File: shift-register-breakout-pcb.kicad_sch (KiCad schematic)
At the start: 19 parts, among them J1 Conn_01x07_Socket, J2 Conn_01x08_Socket, J3 Conn_01x08_Socket, J4 Conn_01x08_Socket, J5 Conn_01x08_Socket

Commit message: adding text, fixing some errors.
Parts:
- added LOGO1, LOGO4: **REF, ct-kicad:awesome-logo, symbol ct-kicad:awesome-logo
- added LOGO2, LOGO3: **REF, ct-kicad:qmk-lite, symbol ct-kicad:qmk-lite-logo
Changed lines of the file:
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@@
+    )
+  )
+  (symbol (lib_id "ct-kicad:qmk-lite-logo") (at 55.88 26.67 0) (unit 1)
+    (in_bom no) (on_board yes) (dnp no) (fields_autoplaced)
+    (property "Reference" "LOGO2" (at 58.42 25.4 0)
+      (effects (font (size 1.27 1.27)) (justify left))
+    )
+    (property "Value" "**REF" (at 58.42 27.94 0)
+      (effects (font (size 1.27 1.27)) (justify left))
+    )
+    (property "Footprint" "ct-kicad:qmk-lite" (at 55.88 26.67 0)
+      (effects (font (size 1.27 1.27)) hide)
+    )
+    (property "Datasheet" "" (at 55.88 26.67 0)
+      (effects (font (size 1.27 1.27)) hide)
+    )
+    (instances
+      (project "shift-register-breakout-pcb"
+        (path "/3deab8a1-c8b9-4932-a4cb-ae1a41e6ee5f"
+          (reference "LOGO2") (unit 1)
+        )
+      )
     )
   )
@@
     )
   )
+  (symbol (lib_id "ct-kicad:awesome-logo") (at 67.31 20.32 0) (unit 1)
+    (in_bom no) (on_board yes) (dnp no) (fields_autoplaced)
+    (property "Reference" "LOGO4" (at 69.85 19.05 0)
+      (effects (font (size 1.27 1.27)) (justify left))
+    )
+    (property "Value" "**REF" (at 69.85 21.59 0)
+      (effects (font (size 1.27 1.27)) (justify left))
+    )
+    (property "Footprint" "ct-kicad:awesome-logo" (at 67.31 20.32 0)
+      (effects (font (size 1.27 1.27)) hide)
+    )
+    (property "Datasheet" "" (at 67.31 20.32 0)
+      (effects (font (size 1.27 1.27)) hide)
+    )
+    (instances
+      (project "shift-register-breakout-pcb"
+        (path "/3deab8a1-c8b9-4932-a4cb-ae1a41e6ee5f"
+          (reference "LOGO4") (unit 1)
+        )
+      )
+    )
+  )
   (symbol (lib_id "power:GND") (at 127 102.87 180) (unit 1)
     (in_bom yes) (on_board yes) (dnp no) (fields_autoplaced)
@@
     )
   )
+  (symbol (lib_id "ct-kicad:awesome-logo") (at 55.88 20.32 0) (unit 1)
+    (in_bom no) (on_board yes) (dnp no) (fields_autoplaced)
+    (property "Reference" "LOGO1" (at 58.42 19.05 0)
+      (effects (font (size 1.27 1.27)) (justify left))
+    )
+    (property "Value" "**REF" (at 58.42 21.59 0)
+      (effects (font (size 1.27 1.27)) (justify left))
+    )
+    (property "Footprint" "ct-kicad:awesome-logo" (at 55.88 20.32 0)
+      (effects (font (size 1.27 1.27)) hide)
+    )
+    (property "Datasheet" "" (at 55.88 20.32 0)
+      (effects (font (size 1.27 1.27)) hide)
+    )
+    (instances
+      (project "shift-register-breakout-pcb"
+        (path "/3deab8a1-c8b9-4932-a4cb-ae1a41e6ee5f"
+          (reference "LOGO1") (unit 1)
+        )
+      )
+    )
+  )
   (symbol (lib_id "Mechanical:MountingHole") (at 22.86 20.32 0) (unit 1)
     (in_bom yes) (on_board yes) (dnp no) (fields_autoplaced)
@@
         )
       )
+    )
+  )
+  (symbol (lib_id "ct-kicad:qmk-lite-logo") (at 67.31 26.67 0) (unit 1)
+    (in_bom no) (on_board yes) (dnp no) (fields_autoplaced)
+    (property "Reference" "LOGO3" (at 69.85 25.4 0)
+      (effects (font (size 1.27 1.27)) (justify left))
+    )
+    (property "Value" "**REF" (at 69.85 27.94 0)
+      (effects (font (size 1.27 1.27)) (justify left))
+    )
+    (property "Footprint" "ct-kicad:qmk-lite" (at 67.31 26.67 0)
+      (effects (font (size 1.27 1.27)) hide)
+    )
+    (property "Datasheet" "" (at 67.31 26.67 0)
+      (effects (font (size 1.27 1.27)) hide)
+    )
+    (instances
+      (project "shift-register-breakout-pcb"
+        (path "/3deab8a1-c8b9-4932-a4cb-ae1a41e6ee5f"
+          (reference "LOGO3") (unit 1)
+        )
+      )

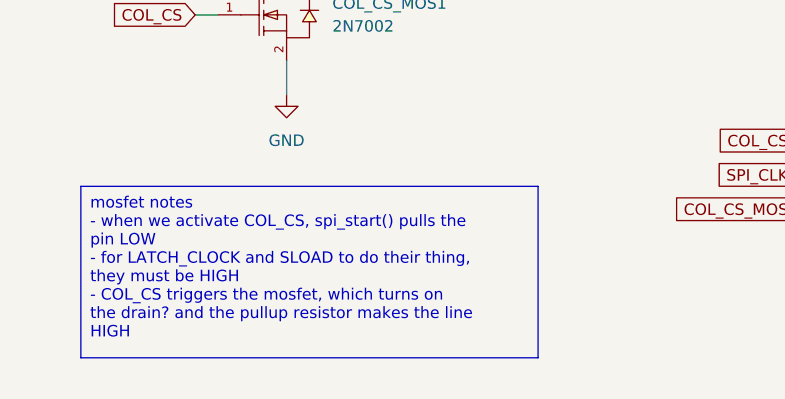
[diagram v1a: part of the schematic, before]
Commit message: fixing mosfet notes in schematic as per burkfers, final pcb notation added
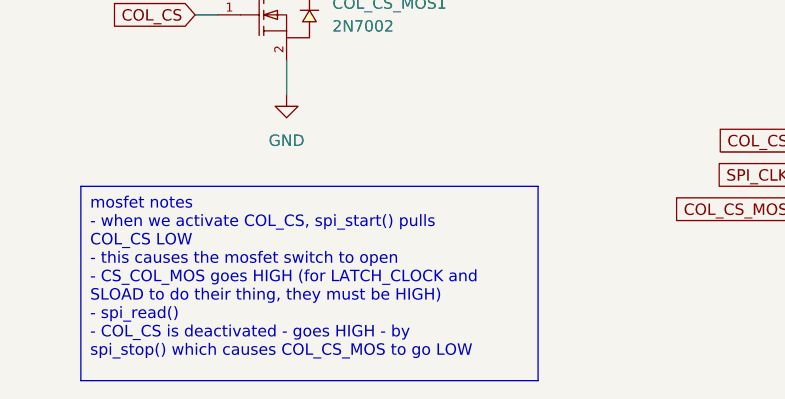
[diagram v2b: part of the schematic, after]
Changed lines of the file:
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@@
     (stroke (width 0) (type default))
   )
-  (text_box "mosfet notes\n- when we activate COL_CS, spi_start() pulls the pin LOW\n- for LATCH_CLOCK and SLOAD to do their thing, they must be HIGH\n- COL_CS triggers the mosfet, which turns on the drain? and the pullup resistor makes the line HIGH"
-    (at 27.94 144.78 0) (size 50.8 19.05)
+  (text_box "mosfet notes\n- when we activate COL_CS, spi_start() pulls COL_CS LOW\n- this causes the mosfet switch to open\n- CS_COL_MOS goes HIGH (for LATCH_CLOCK and SLOAD to do their thing, they must be HIGH)\n- spi_read()\n- COL_CS is deactivated - goes HIGH - by spi_stop() which causes COL_CS_MOS to go LOW"
+    (at 27.94 144.78 0) (size 50.8 21.59)
     (stroke (width 0) (type default))
     (fill (type none))

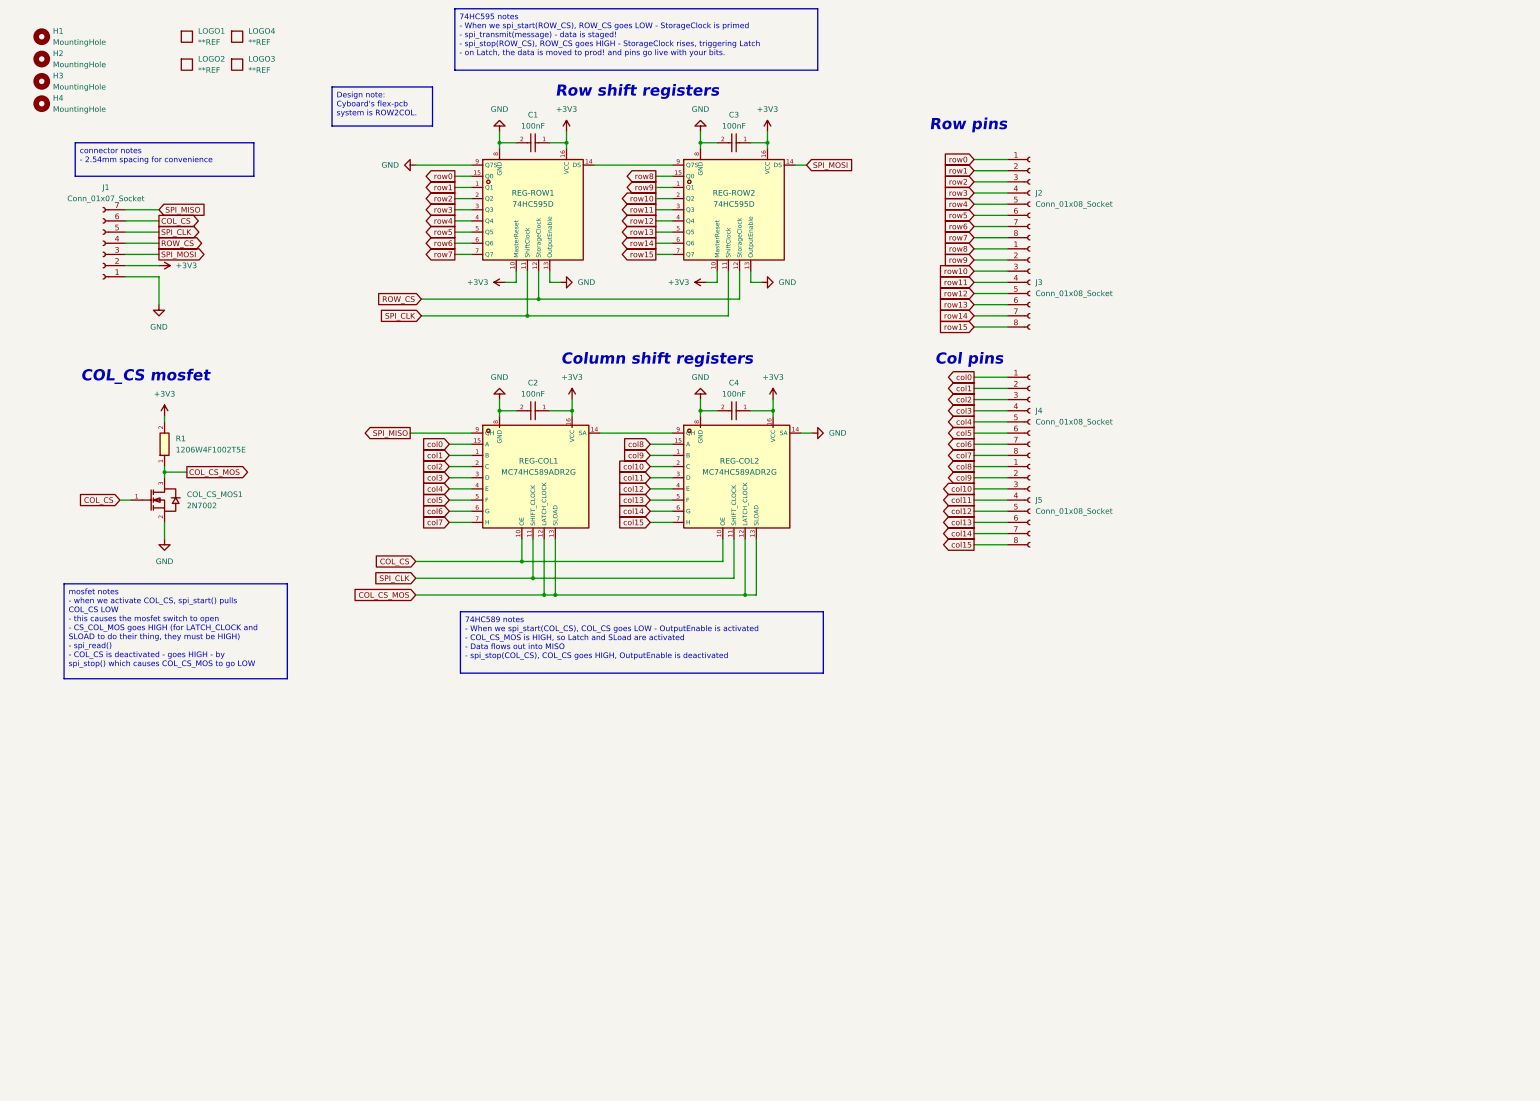
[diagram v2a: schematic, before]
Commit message: adding latch circuit and resistor arrays
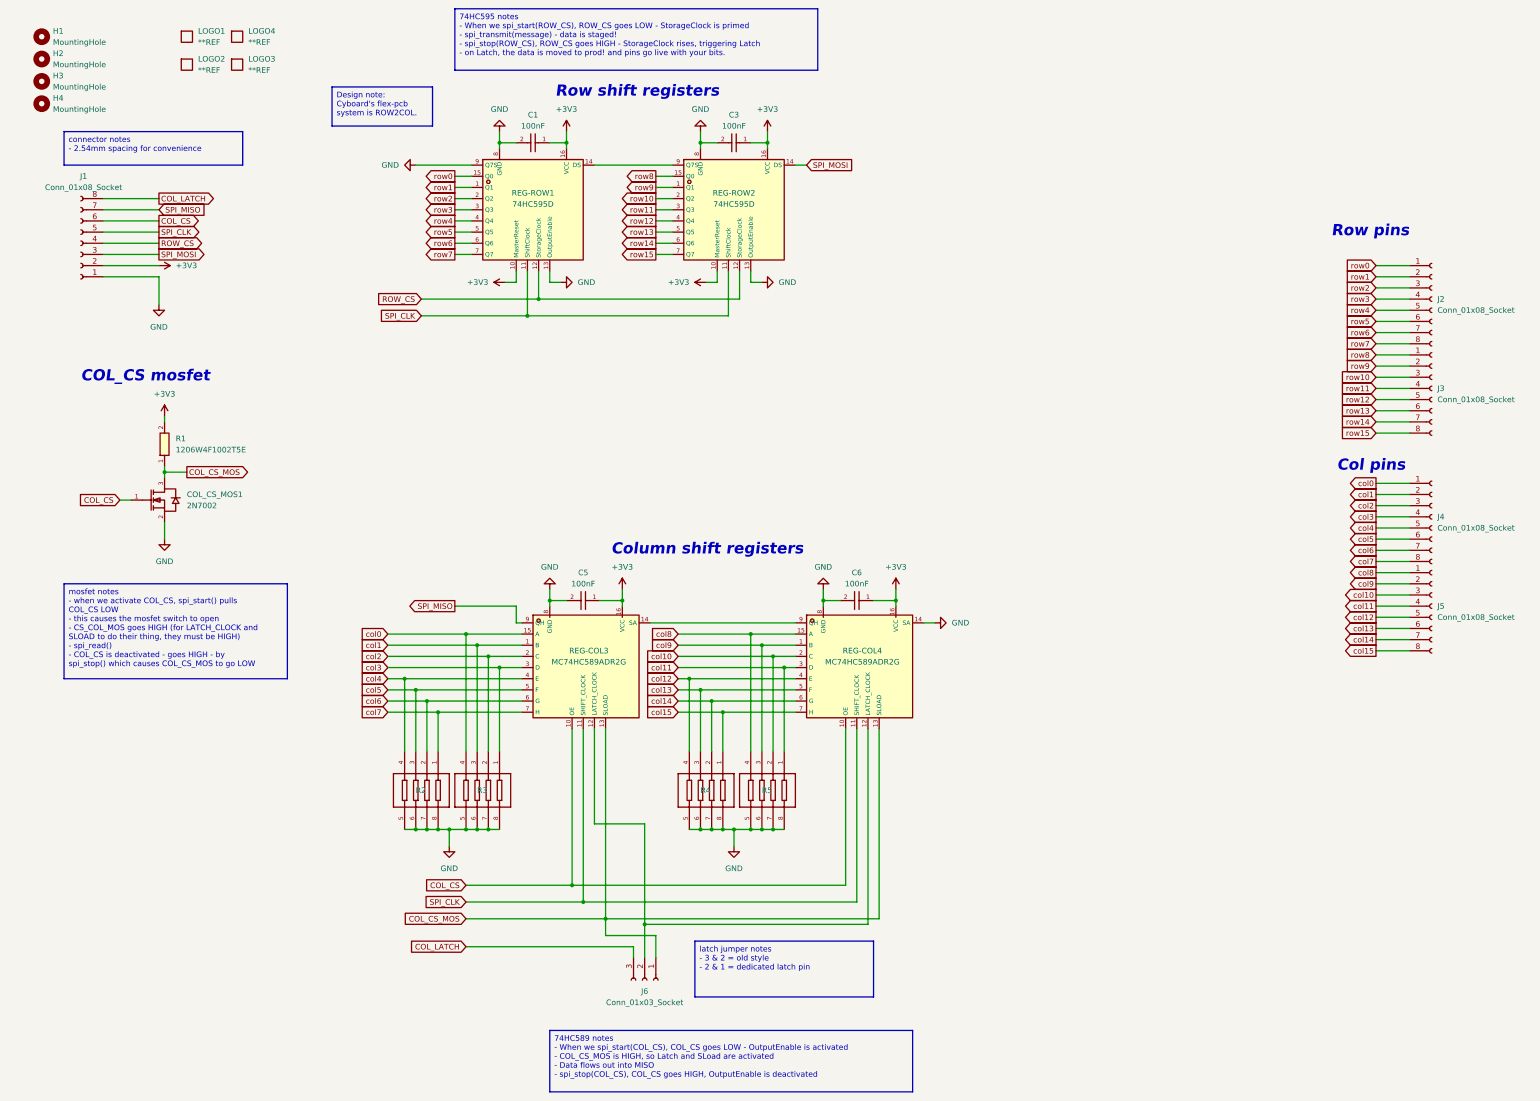
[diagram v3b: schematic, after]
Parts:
- removed C2, C4: 100nF, ct-kicad:C0402, symbol ct-kicad:CL05B104KO5NNNC
- removed REG-COL1, REG-COL2: MC74HC589ADR2G, ct-kicad:SOIC-16_L9.9-W3.9-P1.27-LS6.0-BL, symbol ct-kicad:MC74HC589ADR2G
- added C5, C6: 100nF, ct-kicad:C0402, symbol ct-kicad:CL05B104KO5NNNC
- added J6: Conn_01x03_Socket, Connector_PinHeader_2.54mm:PinHeader_1x03_P2.54mm_Vertical, symbol Connector:Conn_01x03_Socket
- added R2, R3, R4, R5: 4D03WGJ0103T5E, ct-kicad:RES-ARRAY-SMD_0603-8P-L3.2-W1.6-BL, symbol ct-kicad:4D03WGJ0103T5E
- added REG-COL3, REG-COL4: MC74HC589ADR2G, ct-kicad:SOIC-16_L9.9-W3.9-P1.27-LS6.0-BL, symbol ct-kicad:MC74HC589ADR2G
- J1: value Conn_01x07_Socket -> Conn_01x08_Socket; footprint Connector_PinSocket_2.54mm:PinSocket_1x07_P2.54mm_Vertical -> Connector_PinSocket_2.54mm:PinSocket_1x08_P2.54mm_Vertical; symbol Connector:Conn_01x07_Socket -> Connector:Conn_01x08_Socket
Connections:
- net +3V3: now also C5.1, C6.1, REG-COL3.16 (VCC), REG-COL4.16 (VCC)
- net COL_CS: now also REG-COL3.10 (OE), REG-COL4.10 (OE)
- net COL_CS_MOS: now also J6.1 (Pin_1), REG-COL3.13 (SLOAD), REG-COL4.13 (SLOAD)
- net GND: now also C5.2, C6.2, R2.5, R2.6, R2.7, R2.8, R3.5, R3.6, R3.7, R3.8, R4.5, R4.6, R4.7, R4.8, R5.5, R5.6, R5.7, R5.8, REG-COL3.8 (GND), REG-COL4.14 (SA), REG-COL4.8 (GND)
- net SPI_CLK: now also REG-COL3.11 (SHIFT_CLOCK), REG-COL4.11 (SHIFT_CLOCK)
- net SPI_MISO: now also REG-COL3.9 (QH)
- net col0: now also R3.4, REG-COL3.15 (A)
- net col1: now also R3.3, REG-COL3.1 (B)
- net col10: now also R5.2, REG-COL4.2 (C)
- net col11: now also R5.1, REG-COL4.3 (D)
- net col12: now also R4.4, REG-COL4.4 (E)
- net col13: now also R4.3, REG-COL4.5 (F)
- net col14: now also R4.2, REG-COL4.6 (G)
- net col15: now also R4.1, REG-COL4.7 (H)
- net col2: now also R3.2, REG-COL3.2 (C)
- net col3: now also R3.1, REG-COL3.3 (D)
- net col4: now also R2.4, REG-COL3.4 (E)
- net col5: now also R2.3, REG-COL3.5 (F)
- net col6: now also R2.2, REG-COL3.6 (G)
- net col7: now also R2.1, REG-COL3.7 (H)
- net col8: now also R5.4, REG-COL4.15 (A)
- net col9: now also R5.3, REG-COL4.1 (B)
- new net: J6.2 (Pin_2), REG-COL3.12 (LATCH_CLOCK), REG-COL4.12 (LATCH_CLOCK)
- new net: REG-COL3.14 (SA), REG-COL4.9 (QH)
- new net COL_LATCH: J1.8 (Pin_8), J6.3 (Pin_3)
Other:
- moved on the sheet: J2, J3, J4, J5

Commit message: vik-i-fying the design
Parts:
- removed H2, H3, H4: MountingHole, MountingHole:MountingHole_3.2mm_M3_Pad_Via, symbol Mechanical:MountingHole
- added FID1: Fiducial, vik:vik-logo-small, symbol Mechanical:Fiducial
- added J7: vik-module-connector, ct-kicad:FPC-SMD_XF2M-1215-1AH, symbol vik:vik-module-connector
- H1: footprint MountingHole:MountingHole_3.2mm_M3_Pad_Via -> vik:vik-module-mounting-large
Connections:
- net +3V3: now also J7.12 (3V3)
- net COL_CS: now also J7.6 (GP_AD1)
- net COL_LATCH: now also J7.4 (GP_AD2)
- net GND: now also J7.11 (GND)
- net ROW_CS: now also J7.3 (SPI_CS)
- net SPI_CLK: now also J7.1 (SCLK)
- net SPI_MISO: now also J7.2 (MISO)
- net SPI_MOSI: now also J7.5 (MOSI)
- no-connect marks 0 -> 4
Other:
- note added: "VIK module connector"
- moved on the sheet: C5, C6, J2, J3, J4, J5, J6, R2, R3, R4, R5, REG-COL3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

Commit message: mostly done vik-ifying it
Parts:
- removed LOGO2, LOGO3: **REF, ct-kicad:qmk-lite, symbol ct-kicad:qmk-lite-logo
- added H2: MountingHole, MountingHole:MountingHole_3mm_Pad_Via, symbol Mechanical:MountingHole
- H1: footprint vik:vik-module-mounting-large -> MountingHole:MountingHole_3mm_Pad_Via
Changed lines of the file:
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@@
 	)
 	(symbol
-		(lib_id "ct-kicad:qmk-lite-logo")
-		(at 55.88 26.67 0)
-		(unit 1)
-		(exclude_from_sim no)
-		(in_bom no)
-		(on_board yes)
-		(dnp no)
-		(fields_autoplaced yes)
-		(property "Reference" "LOGO2"
-			(at 58.42 25.4 0)
-			(effects
-				(font
-					(size 1.27 1.27)
-				)
-				(justify left)
-			)
-		)
-		(property "Value" "**REF"
-			(at 58.42 27.94 0)
-			(effects
-				(font
-					(size 1.27 1.27)
-				)
-				(justify left)
-			)
-		)
-		(property "Footprint" "ct-kicad:qmk-lite"
-			(at 55.88 26.67 0)
-			(effects
-				(font
-					(size 1.27 1.27)
-				)
-				(hide yes)
-			)
-		)
-		(property "Datasheet" ""
-			(at 55.88 26.67 0)
-			(effects
-				(font
-					(size 1.27 1.27)
-				)
-				(hide yes)
-			)
-		)
-		(property "Description" ""
-			(at 55.88 26.67 0)
-			(effects
-				(font
-					(size 1.27 1.27)
-				)
-				(hide yes)
-			)
-		)
-		(instances
-			(project "shift-register-breakout-pcb"
-				(path "/3deab8a1-c8b9-4932-a4cb-ae1a41e6ee5f"
-					(reference "LOGO2")
-					(unit 1)
-				)
-			)
-		)
-	)
-	(symbol
 		(lib_id "power:GND")
 		(at 172.72 161.29 0)
@@
 	(symbol
 		(lib_id "Mechanical:MountingHole")
-		(at 22.86 20.32 0)
+		(at 24.13 29.21 0)
 		(unit 1)
 		(exclude_from_sim no)
@@
 		(dnp no)
 		(fields_autoplaced yes)
-		(property "Reference" "H1"
-			(at 25.4 19.05 0)
+		(property "Reference" "H2"
+			(at 26.67 27.9399 0)
 			(effects
 				(font
@@
 				)
 				(justify left)
+				(hide yes)
 			)
 		)
 		(property "Value" "MountingHole"
-			(at 25.4 21.59 0)
+			(at 26.67 30.4799 0)
 			(effects
 				(font
@@
 			)
 		)
-		(property "Footprint" "vik:vik-module-mounting-large"
-			(at 22.86 20.32 0)
+		(property "Footprint" "MountingHole:MountingHole_3mm_Pad_Via"
+			(at 24.13 29.21 0)
 			(effects
 				(font
@@
 		)
 		(property "Datasheet" "~"
-			(at 22.86 20.32 0)
+			(at 24.13 29.21 0)
 			(effects
 				(font
@@
 			)
 		)
-		(property "Description" ""
-			(at 22.86 20.32 0)
+		(property "Description" "Mounting Hole without connection"
+			(at 24.13 29.21 0)
 			(effects
 				(font
@@
 			(project "shift-register-breakout-pcb"
 				(path "/3deab8a1-c8b9-4932-a4cb-ae1a41e6ee5f"
-					(reference "H1")
+					(reference "H2")
 					(unit 1)
 				)
@@
 	)
 	(symbol
-		(lib_id "ct-kicad:qmk-lite-logo")
-		(at 67.31 26.67 0)
-		(unit 1)
-		(exclude_from_sim no)
-		(in_bom no)
-		(on_board yes)
-		(dnp no)
-		(fields_autoplaced yes)
-		(property "Reference" "LOGO3"
-			(at 69.85 25.4 0)
-			(effects
-				(font
-					(size 1.27 1.27)
-				)
-				(justify left)
-			)
-		)
-		(property "Value" "**REF"
-			(at 69.85 27.94 0)
-			(effects
-				(font
-					(size 1.27 1.27)
-				)
-				(justify left)
-			)
-		)
-		(property "Footprint" "ct-kicad:qmk-lite"
-			(at 67.31 26.67 0)
-			(effects
-				(font
-					(size 1.27 1.27)
-				)
-				(hide yes)
-			)
-		)
-		(property "Datasheet" ""
-			(at 67.31 26.67 0)
-			(effects
-				(font
-					(size 1.27 1.27)
-				)
-				(hide yes)
-			)
-		)
-		(property "Description" ""
-			(at 67.31 26.67 0)
-			(effects
-				(font
-					(size 1.27 1.27)
-				)
-				(hide yes)
-			)
-		)
-		(instances
-			(project "shift-register-breakout-pcb"
-				(path "/3deab8a1-c8b9-4932-a4cb-ae1a41e6ee5f"
-					(reference "LOGO3")
-					(unit 1)
-				)
-			)
-		)
-	)
-	(symbol
 		(lib_id "power:+3V3")
 		(at 142.24 41.91 0)
@@
 					(unit 1)
 				)
+			)
+		)
+	)
+	(symbol
+		(lib_id "Mechanical:MountingHole")
+		(at 24.13 21.59 0)
+		(unit 1)
+		(exclude_from_sim no)
+		(in_bom yes)
+		(on_board yes)
+		(dnp no)
+		(fields_autoplaced yes)
+		(property "Reference" "H1"
+			(at 26.67 20.3199 0)
+			(effects
+				(font
+					(size 1.27 1.27)
+				)
+				(justify left)
+				(hide yes)
+			)
+		)
+		(property "Value" "MountingHole"
+			(at 26.67 22.8599 0)
+			(effects
+				(font
+					(size 1.27 1.27)
+				)
+				(justify left)
+			)
+		)
+		(property "Footprint" "MountingHole:MountingHole_3mm_Pad_Via"
+			(at 24.13 21.59 0)
+			(effects
+				(font
+					(size 1.27 1.27)
+				)
+				(hide yes)
+			)
+		)
+		(property "Datasheet" "~"
+			(at 24.13 21.59 0)
+			(effects
+				(font
+					(size 1.27 1.27)
+				)
+				(hide yes)
+			)
+		)
+		(property "Description" "Mounting Hole without connection"
+			(at 24.13 21.59 0)
+			(effects
+				(font
+					(size 1.27 1.27)
+				)
+				(hide yes)
+			)
+		)
+		(instances
+			(project "shift-register-breakout-pcb"
+				(path "/3deab8a1-c8b9-4932-a4cb-ae1a41e6ee5f"
+					(reference "H1")
+					(unit 1)
+				)

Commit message: final vik version
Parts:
- removed J1: Conn_01x08_Socket, Connector_PinSocket_2.54mm:PinSocket_1x08_P2.54mm_Vertical, symbol Connector:Conn_01x08_Socket
- added FID2: Fiducial, vik:vik-logo-small, symbol Mechanical:Fiducial
- added J1, J8: Conn_01x04_Socket, Connector_JST:JST_XH_B4B-XH-A_1x04_P2.50mm_Vertical, symbol Connector:Conn_01x04_Socket
- added LOGO2: **REF, ct-kicad:shift-reg-qr-10mm, symbol ct-kicad:shift-reg-qr-10mm
- FID1, J6: now left out of the parts list
- J2, J3, J4, J5: footprint Connector_JST:JST_EH_B8B-EH-A_1x08_P2.50mm_Vertical -> Connector_JST:JST_XH_B8B-XH-A_1x08_P2.50mm_Vertical; now left out of the parts list
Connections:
- net +3V3: now also J8.2 (Pin_2)
- net COL_CS: now also J1.2 (Pin_2)
- net COL_LATCH: now also J1.4 (Pin_4)
- net GND: now also J8.1 (Pin_1)
- net ROW_CS: now also J8.4 (Pin_4)
- net SPI_CLK: now also J1.1 (Pin_1)
- net SPI_MISO: now also J1.3 (Pin_3)
- net SPI_MOSI: now also J8.3 (Pin_3)

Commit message: almost done readme
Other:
- note added: "Bits and bobs"
- note added: "VIK alternate"
- note added: "VIK interconnect"
- note removed: "VIK module connector"
- moved on the sheet: C1, C3, C5, C6, COL_CS_MOS1, FID1, FID2, J6, LOGO1, LOGO4, R2, R3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
